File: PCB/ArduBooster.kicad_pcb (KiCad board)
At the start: 2 copper layers, 150.4 x 99.6 mm, 108 parts, among them IC1 ATMEGA328-P, P3 CONTROL, P4 MAIN_CONN, U1 ICL7660, U2 LM358, U3 4052, X1 CRYSTAL

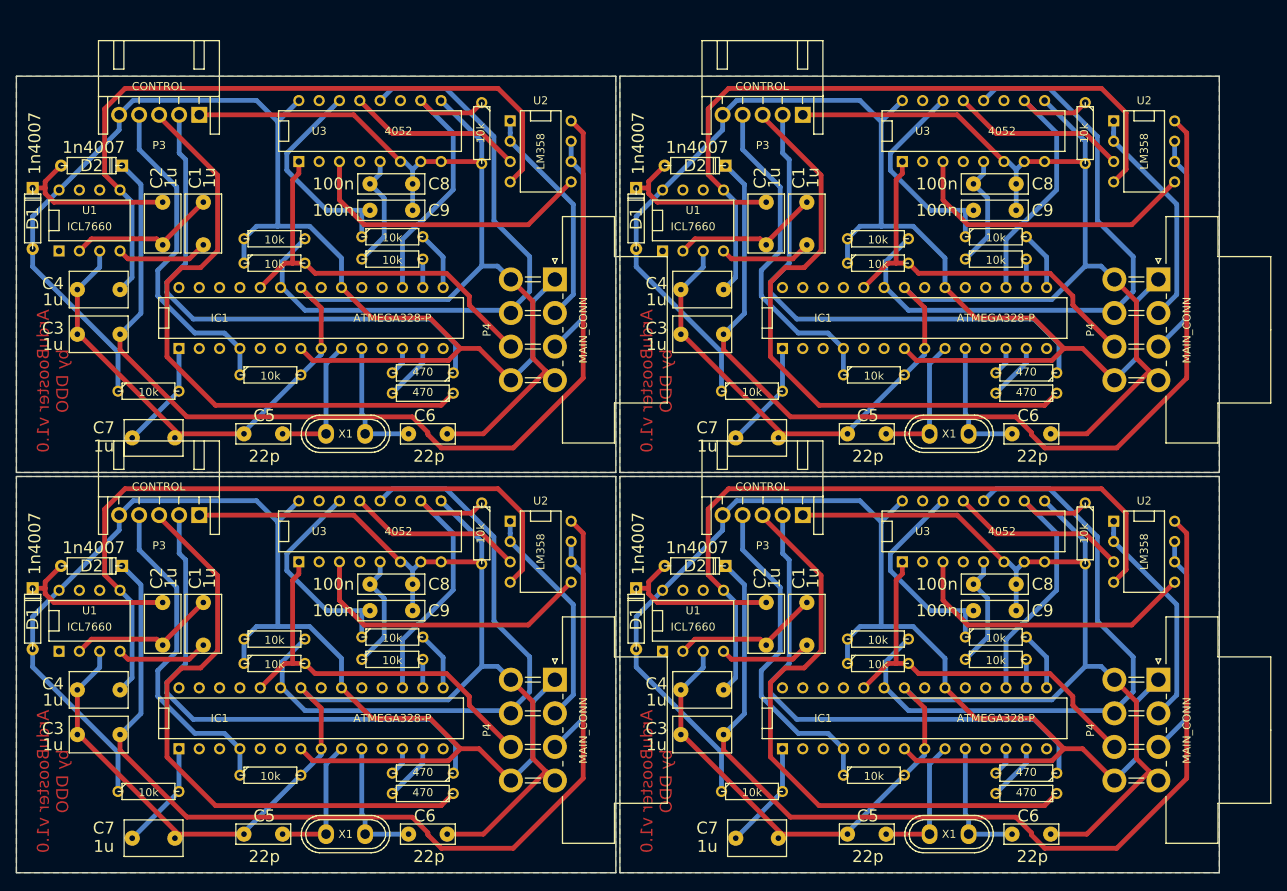
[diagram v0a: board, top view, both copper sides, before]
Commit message: Initial new board route.
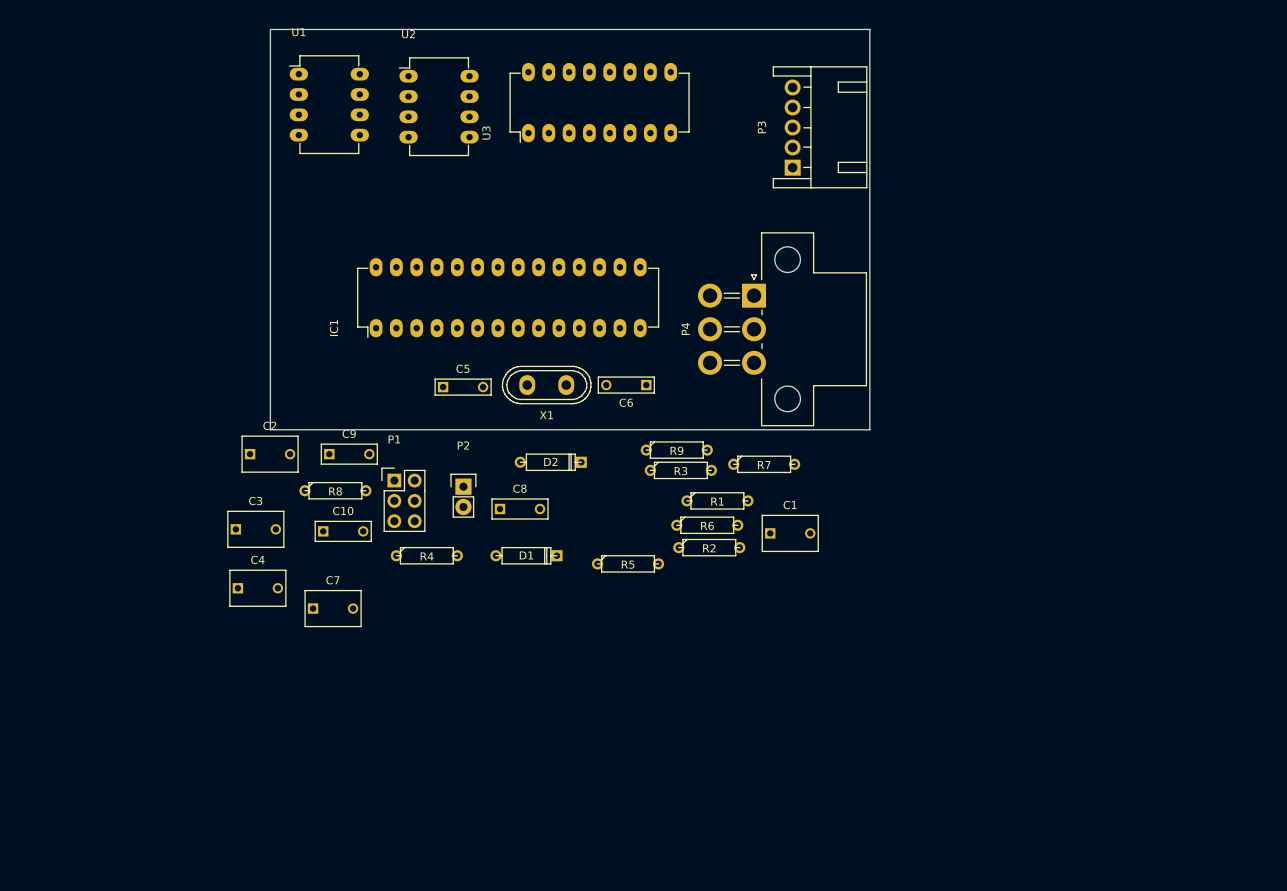
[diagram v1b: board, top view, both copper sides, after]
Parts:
- removed the C1 at (169.7, 61.2)
- removed the C1 at (94.2, 61.2)
- removed the C1 at (169.7, 111.3)
- removed the C1 at (94.2, 111.3)
- removed the C2 at (164.6, 61.2)
- removed the C2 at (89.2, 61.2)
- removed the C2 at (164.6, 111.3)
- removed the C2 at (89.2, 111.3)
- removed the C3 at (159.5, 71.9)
- removed the C3 at (84.1, 71.9)
- removed the C3 at (159.5, 121.9)
- removed the C3 at (84.1, 121.9)
- removed the C4 at (159.5, 66.3)
- removed the C4 at (84.1, 66.3)
- removed the C4 at (159.5, 116.3)
- removed the C4 at (84.1, 116.3)
- removed the C5 at (180.1, 89.4)
- removed the C5 at (104.6, 89.4)
- removed the C5 at (180.1, 139.4)
- removed the C5 at (104.6, 139.4)
- removed the C6 at (200.9, 85.3)
- removed the C6 at (125.5, 85.3)
- removed the C6 at (200.9, 135.4)
- removed the C6 at (125.5, 135.4)
- removed the C7 at (166.6, 90.9)
- removed the C7 at (91.2, 90.9)
- removed the C7 at (166.6, 141.0)
- removed the C7 at (91.2, 141.0)
- removed the C8 at (196.3, 58.2)
- removed the C8 at (120.9, 58.2)
- removed the C8 at (196.3, 108.2)
- removed the C8 at (120.9, 108.2)
- removed the C9 at (196.3, 61.5)
- removed the C9 at (120.9, 61.5)
- removed the C9 at (196.3, 111.5)
- removed the C9 at (120.9, 111.5)
- removed the D1 at (153.4, 60.5)
- removed the D1 at (78.0, 60.5)
- removed the D1 at (153.4, 110.5)
- removed the D1 at (78.0, 110.5)
- removed the D2 at (158.8, 55.9)
- removed the D2 at (83.3, 55.9)
- removed the D2 at (158.8, 105.9)
- removed the D2 at (83.3, 105.9)
- removed the IC1 at (186.2, 72.9)
- removed the IC1 at (110.7, 72.9)
- removed the IC1 at (186.2, 122.9)
- removed the IC1 at (110.7, 122.9)
- removed the P3 at (172.2, 47.5)
- removed the P3 at (96.8, 47.5)
- removed the P3 at (172.2, 97.5)
- removed the P3 at (96.8, 97.5)
- removed the P4 at (216.7, 68.1)
- removed the P4 at (141.2, 68.1)
- removed the P4 at (216.7, 118.1)
- removed the P4 at (141.2, 118.1)
- removed the R1 at (207.5, 49.8)
- removed the R1 at (132.1, 49.8)
- removed the R1 at (207.5, 99.8)
- removed the R1 at (132.1, 99.8)
- removed the R2 at (200.2, 79.8)
- removed the R2 at (124.7, 79.8)
- removed the R2 at (200.2, 129.8)
- removed the R2 at (124.7, 129.8)
- removed the R3 at (200.2, 82.3)
- removed the R3 at (124.7, 82.3)
- removed the R3 at (200.2, 132.3)
- removed the R3 at (124.7, 132.3)
- removed the R4 at (165.9, 82.0)
- removed the R4 at (90.4, 82.0)
- removed the R4 at (165.9, 132.1)
- removed the R4 at (90.4, 132.1)
- removed the R5 at (181.1, 80.0)
- removed the R5 at (105.7, 80.0)
- removed the R5 at (181.1, 130.0)
- removed the R5 at (105.7, 130.0)
- removed the R6 at (181.6, 66.0)
- removed the R6 at (106.2, 66.0)
- removed the R6 at (181.6, 116.1)
- removed the R6 at (106.2, 116.1)
- removed the R7 at (181.6, 63.0)
- removed the R7 at (106.2, 63.0)
- removed the R7 at (181.6, 113.0)
- removed the R7 at (106.2, 113.0)
- removed the R8 at (196.3, 62.7)
- removed the R8 at (120.9, 62.7)
- removed the R8 at (196.3, 112.8)
- removed the R8 at (120.9, 112.8)
- removed the R9 at (196.3, 65.5)
- removed the R9 at (120.9, 65.5)
- removed the R9 at (196.3, 115.6)
- removed the R9 at (120.9, 115.6)
- removed the U1 at (158.5, 60.7)
- removed the U1 at (83.1, 60.7)
- removed the U1 at (158.5, 110.7)
- removed the U1 at (83.1, 110.7)
- removed the U2 at (214.9, 52.1)
- removed the U2 at (139.4, 52.1)
- removed the U2 at (214.9, 102.1)
- removed the U2 at (139.4, 102.1)
- removed the U3 at (193.5, 49.5)
- removed the U3 at (118.1, 49.5)
- removed the U3 at (193.5, 99.6)
- removed the U3 at (118.1, 99.6)
- removed the X1 at (190.5, 87.4)
- removed the X1 at (115.1, 87.4)
- removed the X1 at (190.5, 137.4)
- removed the X1 at (115.1, 137.4)
- added C1: 1u, Capacitors_ThroughHole:C_Rect_L7_W4.5_P5, F.Cu at (168.1, 99.8)
- added C10: 100nF, Capacitors_ThroughHole:C_Rect_L7_W2.5_P5, F.Cu at (112.3, 99.6)
- added C2: 1u, Capacitors_ThroughHole:C_Rect_L7_W4.5_P5, F.Cu at (103.1, 89.9)
- added C3: 1u, Capacitors_ThroughHole:C_Rect_L7_W4.5_P5, F.Cu at (101.3, 99.3)
- added C4: 1u, Capacitors_ThroughHole:C_Rect_L7_W4.5_P5, F.Cu at (101.6, 106.7)
- added C5: 22p, Capacitors_ThroughHole:C_Rect_L7_W2_P5, F.Cu at (127.3, 81.5)
- added C6: 22p, Capacitors_ThroughHole:C_Rect_L7_W2_P5, F.Cu at (152.7, 81.3)
- added C7: 1u, Capacitors_ThroughHole:C_Rect_L7_W4.5_P5, F.Cu at (111.0, 109.2)
- added C8: 100n, Capacitors_ThroughHole:C_Rect_L7_W2.5_P5, F.Cu at (134.4, 96.8)
- added C9: 100n, Capacitors_ThroughHole:C_Rect_L7_W2.5_P5, F.Cu at (113.0, 89.9)
- added D1: 1n4007, Discret:D3, F.Cu at (137.7, 102.6)
- added D2: 1n4007, Discret:D3, F.Cu at (140.7, 90.9)
- added IC1: ATMEGA328-P, Housings_DIP:DIP-28_W7.62mm_LongPads, F.Cu at (118.9, 74.2)
- added P1: ISP, Pin_Headers:Pin_Header_Straight_2x03, F.Cu at (121.2, 93.2)
- added P2: DEBUG TX/RX, Pin_Headers:Pin_Header_Straight_1x02, F.Cu at (129.8, 94.0)
- added P3: CONTROL, Connect:Wafer_Horizontal15x5.8x7RM2.5-5, F.Cu at (170.9, 54.1)
- added P4: MAIN_CONN, Connectors_Molex:Molex_MiniFit-JR-5569-06A1_2x03x4.20mm_Angled, F.Cu at (166.1, 70.1)
- added R1: 10k, Discret:R3, F.Cu at (161.5, 95.8)
- added R2: 470, Discret:R3, F.Cu at (160.5, 101.6)
- added R3: 470, Discret:R3, F.Cu at (157.0, 91.9)
- added R4: 10k, Discret:R3, F.Cu at (125.2, 102.6)
- added R5: 10k, Discret:R3, F.Cu at (150.4, 103.6)
- added R6: 10k, Discret:R3, F.Cu at (160.3, 98.8)
- added R7: 10k, Discret:R3, F.Cu at (167.4, 91.2)
- added R8: 10k, Discret:R3, F.Cu at (113.8, 94.5)
- added R9: 10k, Discret:R3, F.Cu at (156.5, 89.4)
- added U1: ICL7660, Housings_DIP:DIP-8_W7.62mm_LongPads, F.Cu at (109.2, 42.4)
- added U2: LM358, Housings_DIP:DIP-8_W7.62mm_LongPads, F.Cu at (122.9, 42.7)
- added U3: 4052, Housings_DIP:DIP-16_W7.62mm_LongPads, F.Cu at (137.9, 49.8)
- added X1: CRYSTAL, Crystals:Crystal_HC50-U_Vertical, F.Cu at (140.2, 81.3)
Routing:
- net GNDREF: track 751.5 -> 0.00 mm
- net +5V: track 660.8 -> 0.00 mm
- net /Doubler_Inverter/+9V: track 498.4 -> 0.00 mm
- net /Doubler_Inverter/-5V: track 353.9 -> 0.00 mm
- net /Base Arduino/CH0_PEDAL_SIG: track 317.8 -> 0.00 mm
- net /Base Arduino/LED2: track 304.9 -> 0.00 mm
- net /Base Arduino/LED1: track 264.0 -> 0.00 mm
- net /Base Arduino/CH1_PEDAL_SIG: track 202.4 -> 0.00 mm
- net /Base Arduino/SWITCH: track 167.5 -> 0.00 mm
- net /Isolator/CH1_MUXDEMUX_OUT: track 149.1 -> 0.00 mm
- net /Base Arduino/OUTPUT_SELECTION: track 146.1 -> 0.00 mm
- net /Connectors/CH0_OUT: track 112.9 -> 0.00 mm
- net /Connectors/CH1_OUT: track 111.0 -> 0.00 mm
- net /Base Arduino/CH0_ARDUINO_SIG: track 108.8 -> 0.00 mm
- net /Isolator/CH0_MUXDEMUX_OUT: track 87.8 -> 0.00 mm
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- removed copper zone on B.Cu, net GNDREF
- removed copper zone on F.Cu, net GNDREF
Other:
- board size 150.4 x 99.6 mm -> 74.9 x 50 mm
- board text removed: "ArduBooster v1.0 by DDO"

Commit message: First components placement.
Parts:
- moved R8 70.8 mm to (165.4, 46.0), turned to 270 degrees
- moved C1 69.2 mm to (114.3, 56.4), turned to 180 degrees
- moved C9 67.0 mm to (161.3, 43.4), turned to 270 degrees
- moved C10 62.9 mm to (160.5, 59.2)
- moved C4 52.9 mm to (117.9, 56.4)
- moved C3 52.4 mm to (131.3, 56.4), turned to 180 degrees
- moved R5 50.8 mm to (162.6, 54.4), turned to 180 degrees
- moved C8 44.3 mm to (148.1, 54.6)
- moved D1 43.2 mm to (121.7, 62.5), turned to 180 degrees
- moved R6 40.0 mm to (143.5, 62.5), turned to 180 degrees
- moved R7 31.7 mm to (153.9, 62.5)
- moved R9 31.1 mm to (150.4, 58.9)
- moved C7 30.6 mm to (108.7, 78.7)
- moved C2 29.9 mm to (114.3, 62.2), turned to 180 degrees
- moved D2 29.6 mm to (132.6, 62.5)
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
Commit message: Routing...
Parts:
- moved R8 28.1 mm to (140.5, 58.9), turned to 0 degrees
- moved P4 25.1 mm to (166.1, 45.0)
- moved P3 24.9 mm to (170.9, 79.0)
- moved R5 21.3 mm to (162.1, 75.7), turned to 270 degrees
- moved C9 15.9 mm to (148.1, 52.3), turned to 0 degrees
- moved C10 8.81 mm to (165.4, 66.5), turned to 180 degrees
- moved U2 7.18 mm to (130.0, 41.7), turned to 270 degrees
- moved D1 7.16 mm to (115.3, 65.8), turned to 90 degrees
- moved C1 4.44 mm to (110.2, 58.2), turned to 90 degrees
- moved C2 1.55 mm to (112.8, 62.5)
- moved C8 1.27 mm to (148.1, 55.9)
- moved U3 1.27 mm to (137.9, 48.5)
- moved U1 1.02 mm to (109.2, 41.4)
- moved IC1 0.51 mm to (119.4, 74.2)
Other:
- net class Default: clearance 0.5 -> 0.3; trace_width 0.6 -> 0.3
- rule trace_clearance: 0.5 -> 0.3

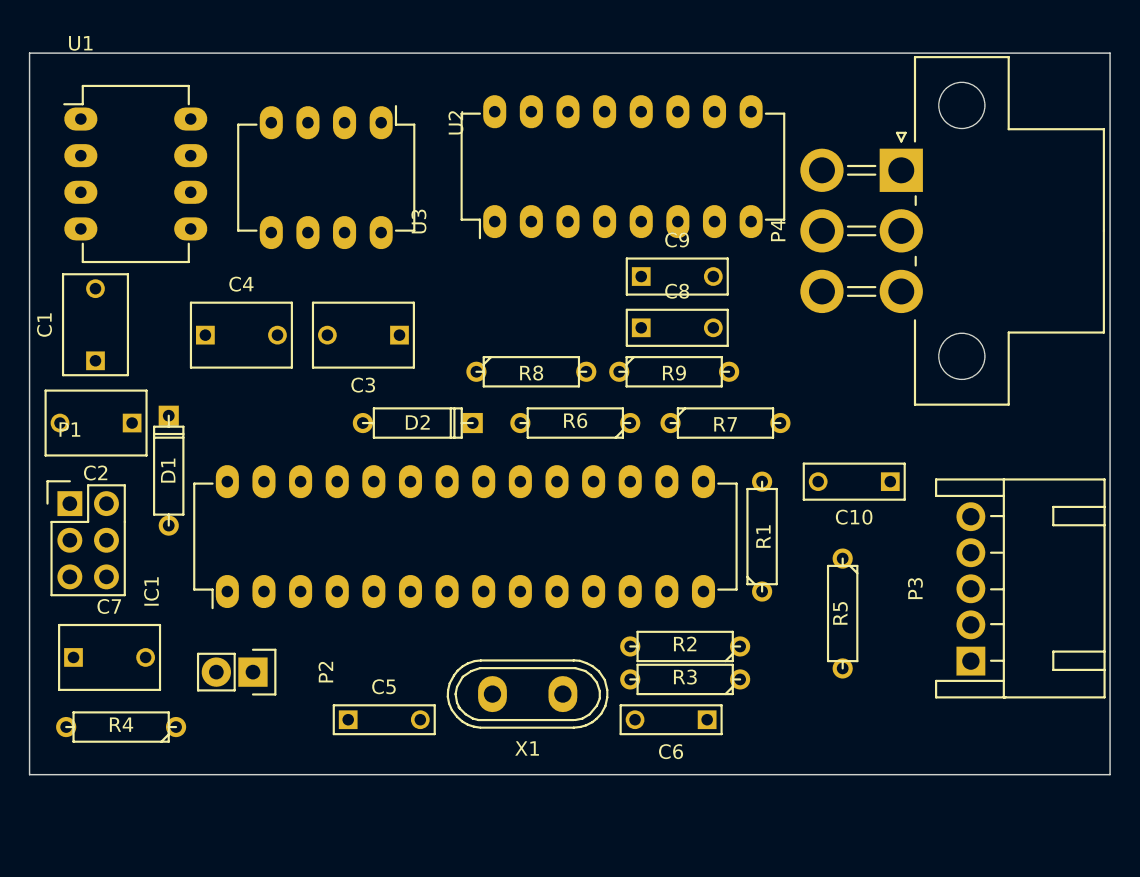
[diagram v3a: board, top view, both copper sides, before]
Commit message: New crystal footprint. New route.
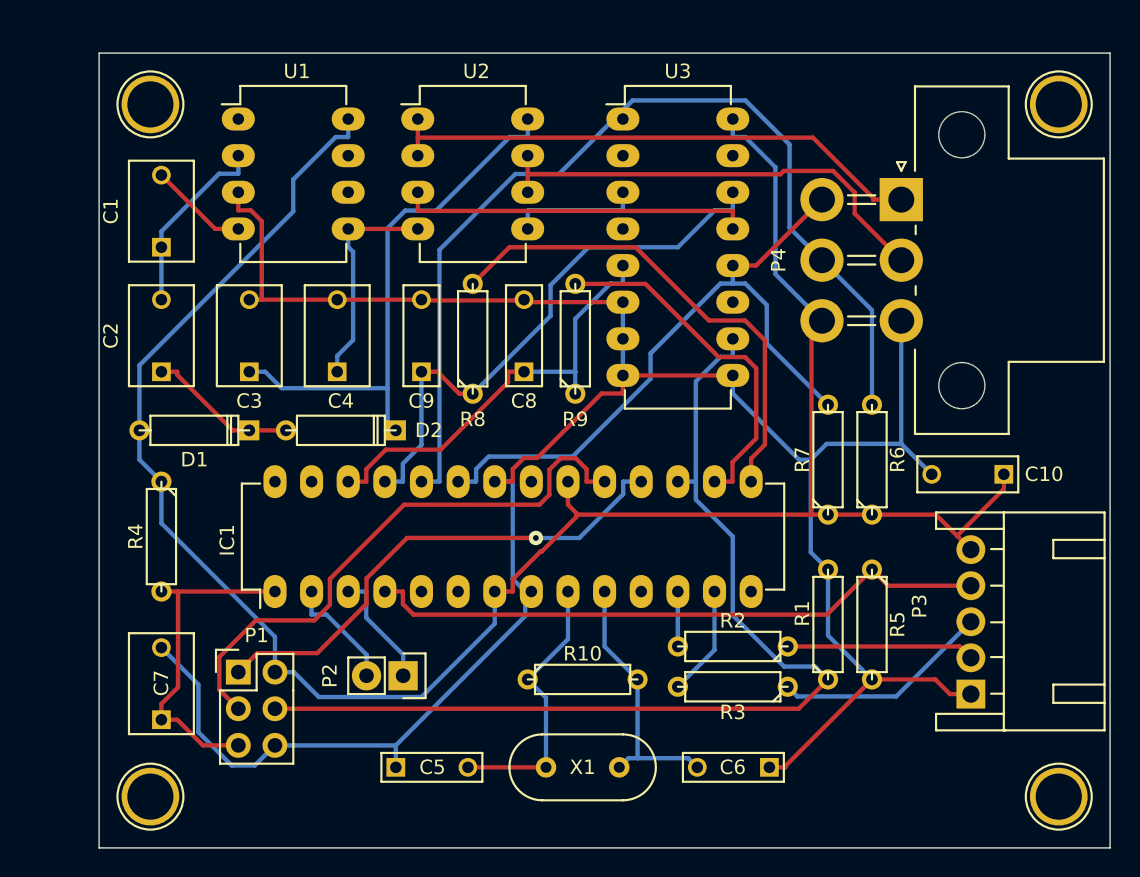
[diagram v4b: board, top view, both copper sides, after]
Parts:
- added H1: , Connect:1pin, F.Cu at (177.0, 40.4)
- added H2: , Connect:1pin, F.Cu at (177.0, 88.4)
- added H3: , Connect:1pin, F.Cu at (114.0, 40.4)
- added H4: , Connect:1pin, F.Cu at (114.0, 88.4)
- added R10: 1M, Discret:R3, F.Cu at (144.0, 80.3)
- C10: value 100nF -> 100n
- X1: footprint Crystals:Crystal_HC50-U_Vertical -> Crystals:HC-49V
- moved R6 20.7 mm to (164.1, 65.0), turned to 90 degrees
- moved C9 16.6 mm to (132.8, 58.9), turned to 90 degrees
- moved P1 16.5 mm to (120.1, 79.8)
- moved R4 13.5 mm to (114.8, 70.4), turned to 270 degrees
- moved U3 11.4 mm to (146.8, 41.4), turned to 0 degrees
- moved U1 10.9 mm to (120.1, 41.4)
- moved C3 10.7 mm to (120.9, 58.9), turned to 90 degrees
- moved P2 10.4 mm to (131.6, 80.0)
- moved C4 9.49 mm to (127.0, 58.9), turned to 90 degrees
- moved C1 9.11 mm to (114.8, 50.3)
- moved C8 8.68 mm to (140.0, 58.9), turned to 90 degrees
- moved X1 8.13 mm to (146.6, 86.4)
- moved C10 7.89 mm to (173.2, 66.0)
- moved R1 7.62 mm to (161.0, 76.5)
- moved R7 7.55 mm to (161.0, 65.0), turned to 90 degrees
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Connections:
- IC1 pad 25: Net-(IC1-Pad25) -> /Base Arduino/CH0_ARDUINO_SIG
- IC1 pad 26: Net-(IC1-Pad26) -> /Base Arduino/CH1_ARDUINO_SIG
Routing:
- net GNDREF: track 0.00 -> 169.0 mm
- net +5V: track 0.00 -> 144.9 mm
- net /Base Arduino/MOSI: track 0.00 -> 70.7 mm
- net /Base Arduino/CH1_PEDAL_SIG: track 0.00 -> 68.2 mm
- net /Base Arduino/CH0_PEDAL_SIG: track 0.00 -> 47.2 mm
- net /Base Arduino/SWITCH: track 0.00 -> 43.6 mm
- net /Base Arduino/SCK: track 0.00 -> 39.8 mm
- net /Base Arduino/CH0_ARDUINO_SIG: track 0.00 -> 39.4 mm
- net /Doubler_Inverter/+9V: track 0.00 -> 38.2 mm
- net /Connectors/CH0_OUT: track 0.00 -> 37.9 mm
- net /Base Arduino/MISO: track 0.00 -> 35.0 mm, vias 0 -> 1
- net Net-(IC1-Pad15): track 0.00 -> 34.2 mm
- net /Connectors/CH1_OUT: track 0.00 -> 32.0 mm
- net /Base Arduino/CH1_ARDUINO_SIG: track 0.00 -> 30.6 mm
- net Net-(IC1-Pad16): track 0.00 -> 24.8 mm
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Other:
- board size 74.9 x 50 mm -> 70.1 x 55.1 mm
